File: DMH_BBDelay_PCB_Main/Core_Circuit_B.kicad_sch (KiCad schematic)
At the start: 74 parts, among them J30 Conn_01x08, J31 Conn_01x08, J32 Conn_01x08, J33 Conn_01x08, Q8 J113, SW1 SW_DPDT_3way_x2, SW2 SW_DPDT_x2, SW4 SW_SPDT, U18 CD4053B, U5 TL074, U6 TL074, U7 V3205, U8 CD4046, U9 40106

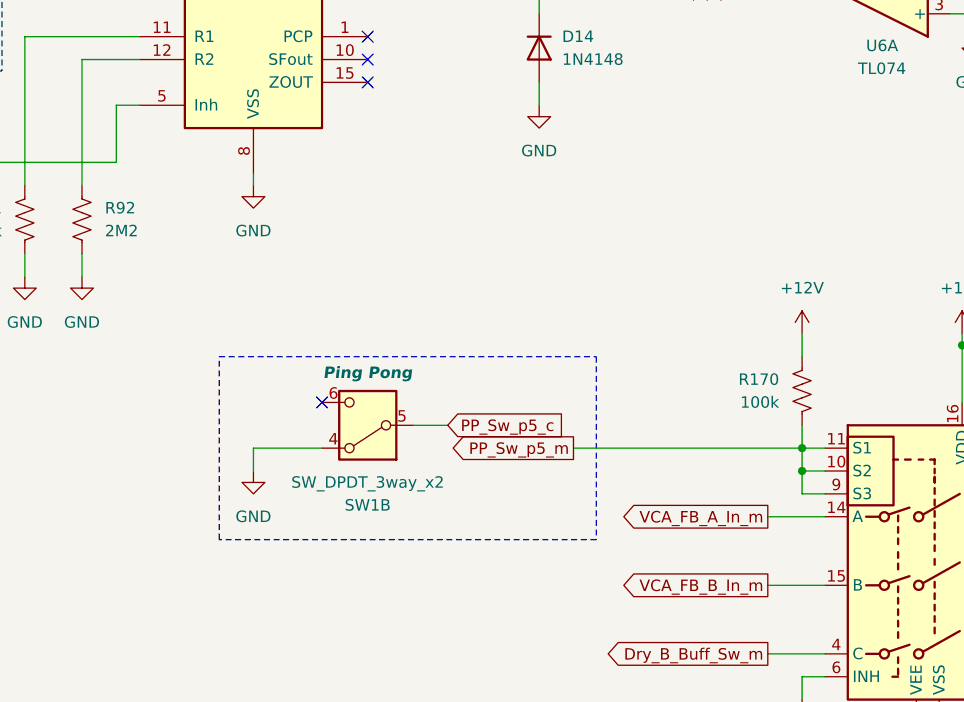
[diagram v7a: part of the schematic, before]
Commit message: Connected blue LED to Ping Pong switch
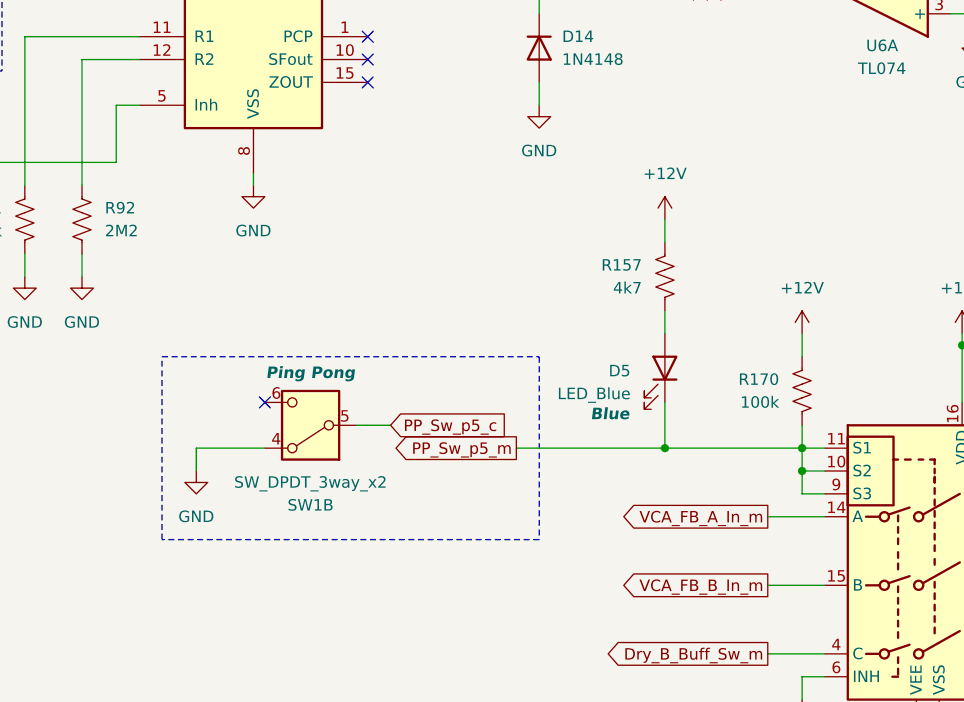
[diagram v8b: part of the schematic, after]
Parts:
- added D5: LED_Blue, LED_THT:LED_D3.0mm, symbol Device:LED
- added R157: 4k7, Resistor_THT:R_Axial_DIN0207_L6.3mm_D2.5mm_P7.62mm_Horizontal, symbol Device:R_US
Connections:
- net +12V: now also R157.1
- net PP_Sw_p5_m: now also D5.1 (K)
- new net: D5.2 (A), R157.2
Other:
- moved on the sheet: SW1B
